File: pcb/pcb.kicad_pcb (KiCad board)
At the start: 2 copper layers, 48 x 60 mm, 47 parts, among them J1 USB_C_Receptacle_USB2.0_14P, J2 LCD, J4 LCD CTRL, J5 M SEN, J6 HC-05, J7 DEBUG, J9 USART3 TX, SW1 PWR SWITCH, U1 TLV62569DBV, U2 STM32F446RETx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

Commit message: finish revision 2
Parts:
- added FB1: FerriteBead, muRata BLM21PG121SN1D:BEADC2012X105N, F.Cu at (73.7, 88.9)
- added R10: 1, Resistor_SMD:R_0603_1608Metric_Pad0.98x0.95mm_HandSolder, F.Cu at (74.6, 85.9)
- D2: value SYS LED -> DEBUG LED
- J5: value M SEN -> MOISTURE
- J9: value USART3 TX -> DEBUG TX
- moved C12 1.48 mm to (77.8, 89.9)
- moved D3 1.48 mm to (79.8, 94.4)
- moved BT1 1.48 mm to (89.7, 91.0)
- moved C11 1.48 mm to (84.8, 89.7)
- moved R9 1.48 mm to (79.8, 92.6)
- moved U3 1.48 mm to (81.2, 89.7)
- moved R8 1.48 mm to (82.5, 93.4)
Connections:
- J1 pad A9: +Vext -> Net-(FB1-Pad1)
- J1 pad B9: +Vext -> Net-(FB1-Pad1)
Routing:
- net LCD D1: track 8.84 -> 19.1 mm, vias 1 -> 2
- net Net-(FB1-Pad1): track 0.00 -> 5.92 mm
- net +Vext: track 22.5 -> 16.6 mm
- net +Vbat: track 24.1 -> 19.4 mm
- net Net-(FB1-Pad2): track 0.00 -> 2.09 mm
- net +3.3V: track 94.9 -> 96.3 mm
- net GND: track 16.5 -> 16.7 mm, vias 46 -> 92
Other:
- board text added: "+3.3V"
- board text added: "+5V"
- board text added: "ADC2"
- board text added: "BLE"
- board text added: "CHARGE"
- board text added: "D0"
- board text added: "D1"
- board text added: "D2"
- board text added: "D3"
- board text added: "D4"
- board text added: "D5"
- board text added: "D6"
- board text added: "D7"
- board text added: "GND"
- board text added: "LCD"
- board text added: "LCD E"
- board text added: "LCD RS"
- board text added: "NRST"
- board text added: "POWER"
- board text added: "RX"
- board text added: "SWCLK"
- board text added: "SWDIO"
- board text added: "TX"
- board text added: "V0"
- board text added: "ed123213"

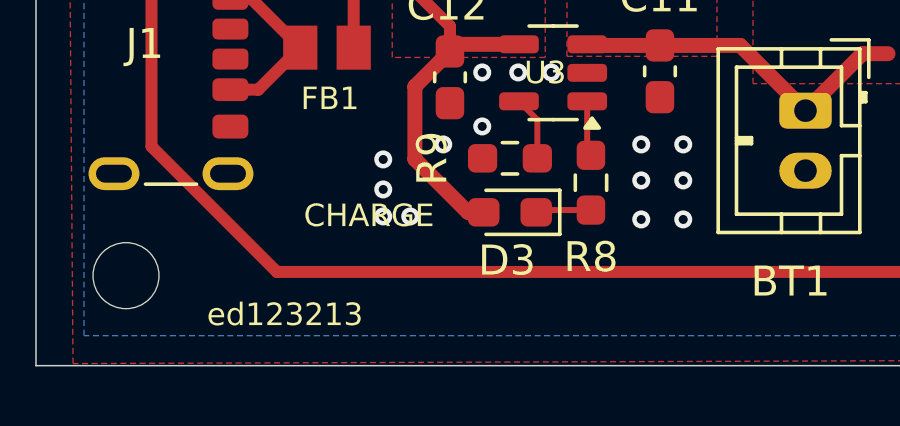
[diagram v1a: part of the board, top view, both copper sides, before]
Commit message: Add rev number to board
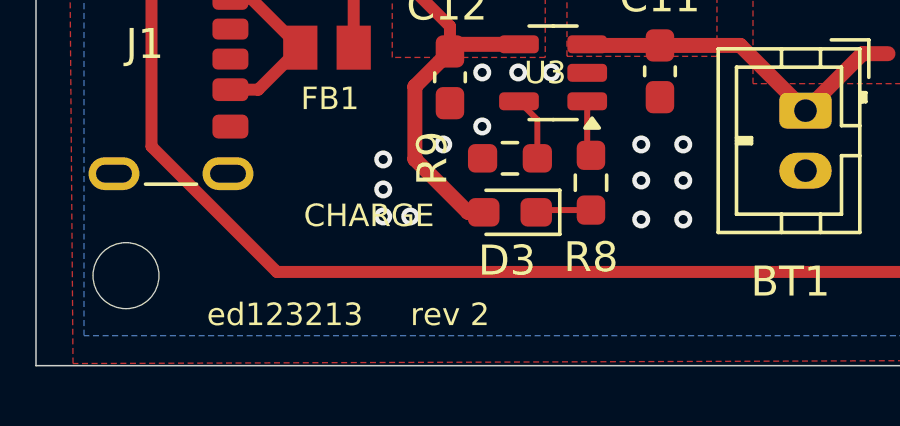
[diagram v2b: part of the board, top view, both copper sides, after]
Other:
- board text added: "rev 2"
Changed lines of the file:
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@@
+		)
+	)
+	(gr_text "rev 2"
+		(at 77.8 97.8 0)
+		(layer "F.SilkS")
+		(effects
+			(font
+				(size 0.75 0.75)
+				(thickness 0.09375)
+			)
 		)
 	)

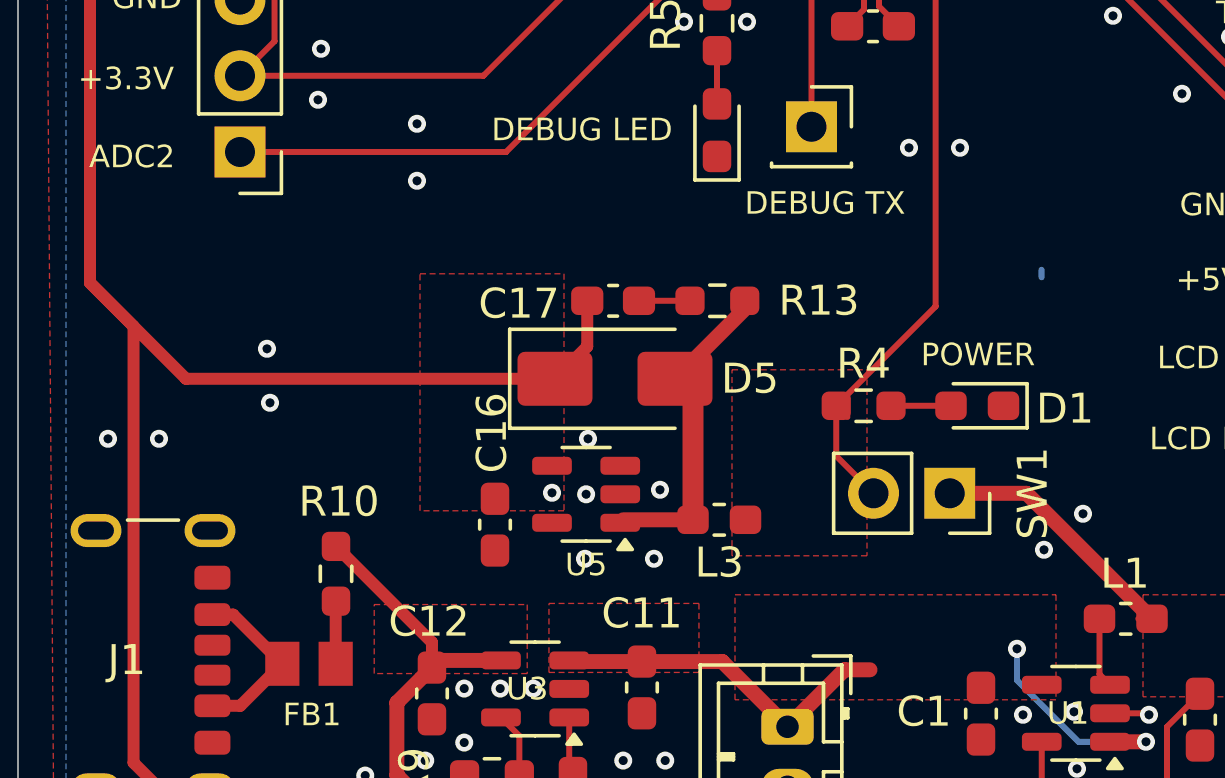
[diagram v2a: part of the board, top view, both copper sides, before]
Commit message: add power plane on boost converter input
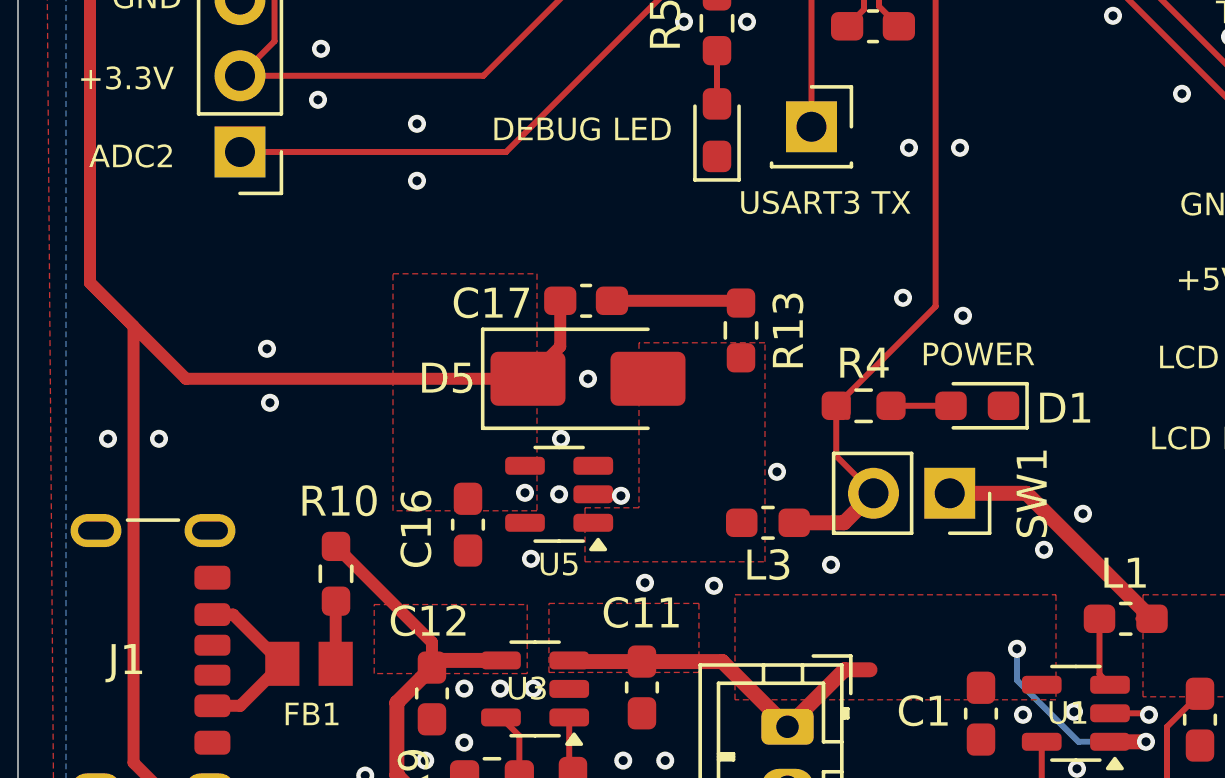
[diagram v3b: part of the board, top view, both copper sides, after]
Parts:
- J9: value DEBUG TX -> USART3 TX
- moved L3 1.63 mm to (89.0, 84.2)
- moved R13 1.26 mm to (88.1, 77.8), turned to 90 degrees
- moved C16 0.90 mm to (79.0, 84.3)
- moved C17 0.90 mm to (82.9, 76.8)
- moved D5 0.90 mm to (83.0, 79.4)
- moved U5 0.90 mm to (82.0, 83.2)
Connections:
- net SYS LED renamed DEBUG LED
- R1 pad 2: +3.3Vswin -> Net-(U1-FB)
- R2 pad 1: +3.3Vswin -> Net-(U1-FB)
- U1 pad 5: +3.3Vswin -> Net-(U1-FB)
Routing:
- net Net-(D5-A): track 11.3 -> 1.26 mm
- net +3.3Vswin: track 21.3 -> 17.5 mm
- net Net-(U1-FB): track 0.00 -> 3.79 mm
- net +3.3V: track 96.3 -> 99.3 mm
- net Net-(C17-Pad1): track 1.70 -> 4.33 mm
- net +5V: track 161.4 -> 160.5 mm
- net GND: track 16.7 -> 16.5 mm, vias 92 -> 98
- added copper zone on F.Cu, net Net-(D5-A)
- removed copper zone on F.Cu, net +3.3V

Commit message: mark pin 1 on stm32f4
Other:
- board text added: "1"
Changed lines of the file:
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@@
+		)
+	)
+	(gr_text "1"
+		(at 85 54.6 0)
+		(layer "F.SilkS")
+		(effects
+			(font
+				(size 0.7 0.7)
+				(thickness 0.15)
+			)
 		)
 	)

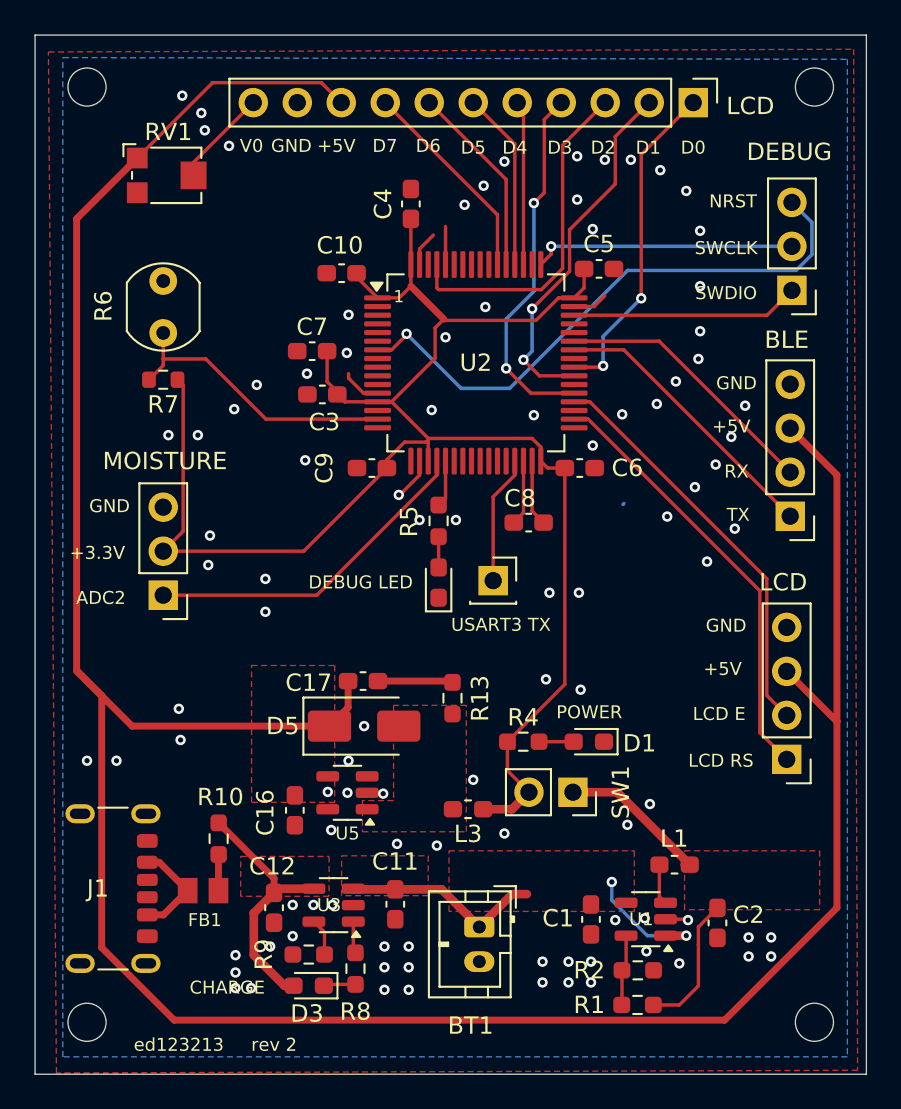
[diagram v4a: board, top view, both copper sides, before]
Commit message: Add battery sensor to pcb
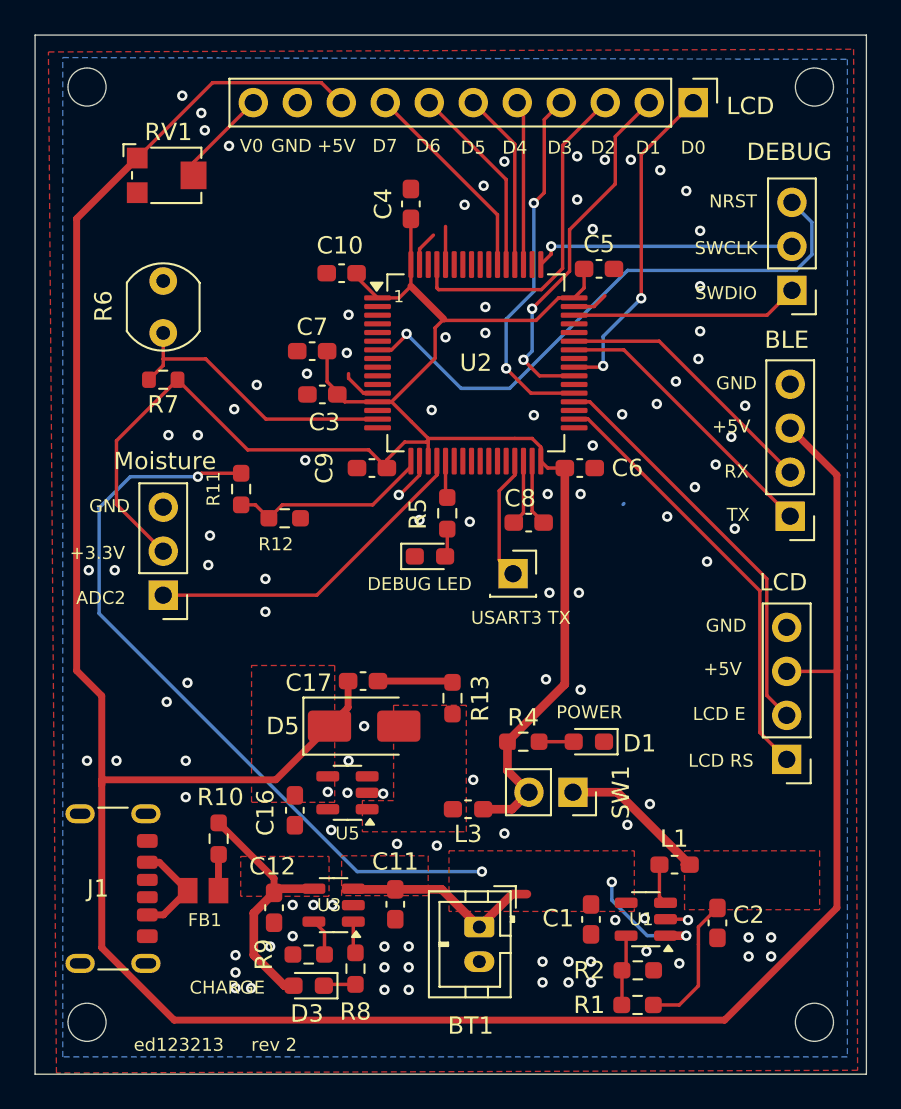
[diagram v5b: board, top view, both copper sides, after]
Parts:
- added R11: 100k, Resistor_SMD:R_0603_1608Metric_Pad0.98x0.95mm_HandSolder, F.Cu at (75.9, 65.7)
- added R12: 100k, Resistor_SMD:R_0603_1608Metric_Pad0.98x0.95mm_HandSolder, F.Cu at (78.4, 67.4)
- J5: value MOISTURE -> Moisture
- moved D2 1.59 mm to (86.8, 69.6), turned to 0 degrees
- moved J9 1.22 mm to (91.6, 70.6)
- moved R5 0.66 mm to (87.8, 67.1)
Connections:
- U2 pad 17: unconnected-(U2-PA3-Pad17) -> ADC3
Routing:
- net +Vbat: track 19.4 -> 62.8 mm, vias 2 -> 4
- net ADC3: track 0.00 -> 11.7 mm
- net +5V: track 160.5 -> 158.1 mm
- net +3.3V: track 99.3 -> 100.6 mm
- net DEBUG LED: track 2.70 -> 2.14 mm
- net GND: vias 98 -> 105

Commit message: Make power traces better on pcb
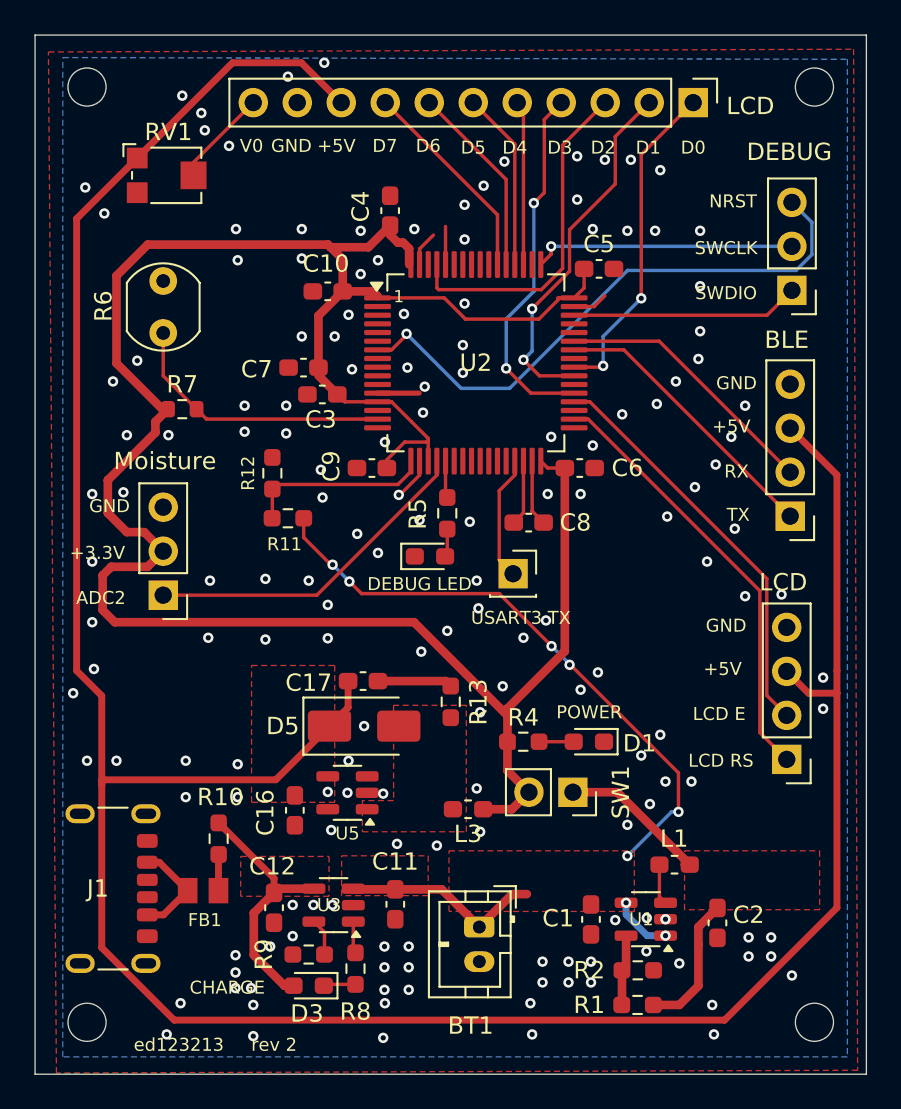
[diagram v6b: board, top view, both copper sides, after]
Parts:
- moved R11 3.18 mm to (78.6, 67.4), turned to 180 degrees
- moved R12 2.70 mm to (77.7, 64.8), turned to 90 degrees
- moved R7 2.02 mm to (72.5, 61.1), turned to 0 degrees
- moved C10 1.32 mm to (80.9, 54.3)
- moved C4 1.26 mm to (84.5, 49.6)
- moved C7 1.07 mm to (79.5, 58.7)
- moved R13 0.23 mm to (88.0, 78.0)
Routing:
- net +3.3V: track 100.6 -> 137.1 mm
- net +Vbat: track 62.8 -> 50.1 mm, vias 4 -> 8
- net +5V: track 158.1 -> 159.5 mm
- net GND: track 16.5 -> 15.2 mm, vias 105 -> 163
- net ADC1: track 16.9 -> 15.9 mm
- net ADC3: track 11.7 -> 10.7 mm

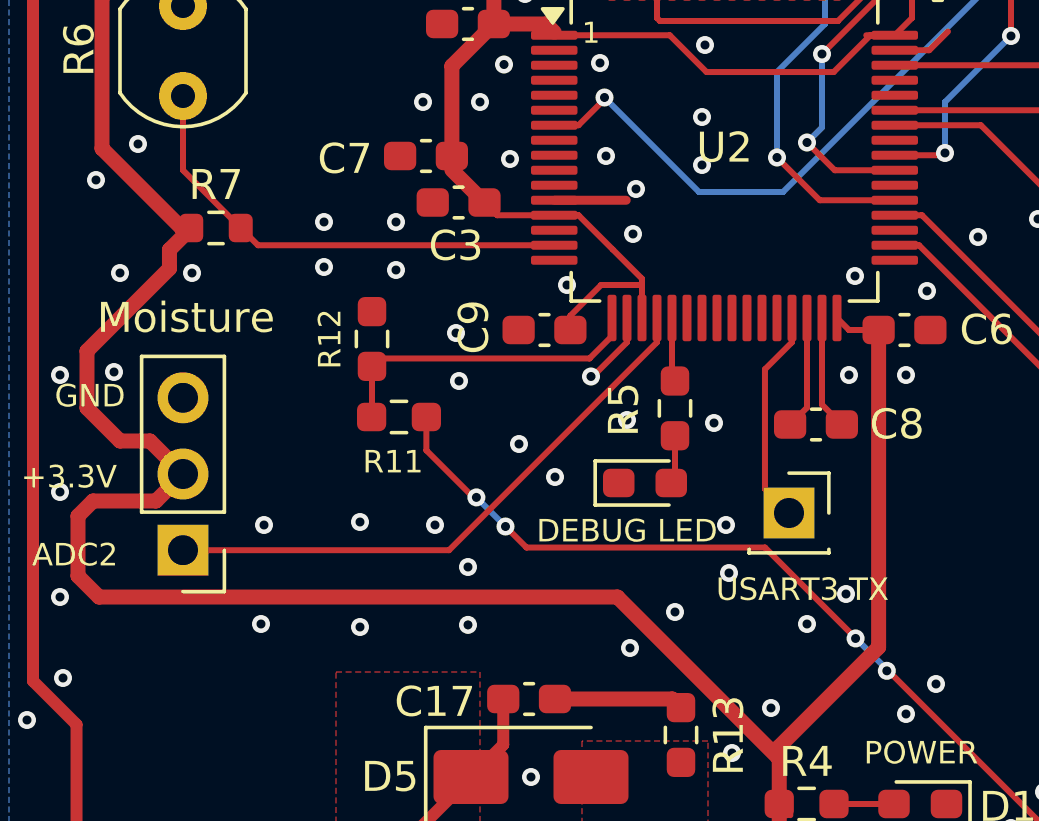
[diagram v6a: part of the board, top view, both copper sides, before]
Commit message: Add pcb export to makefile
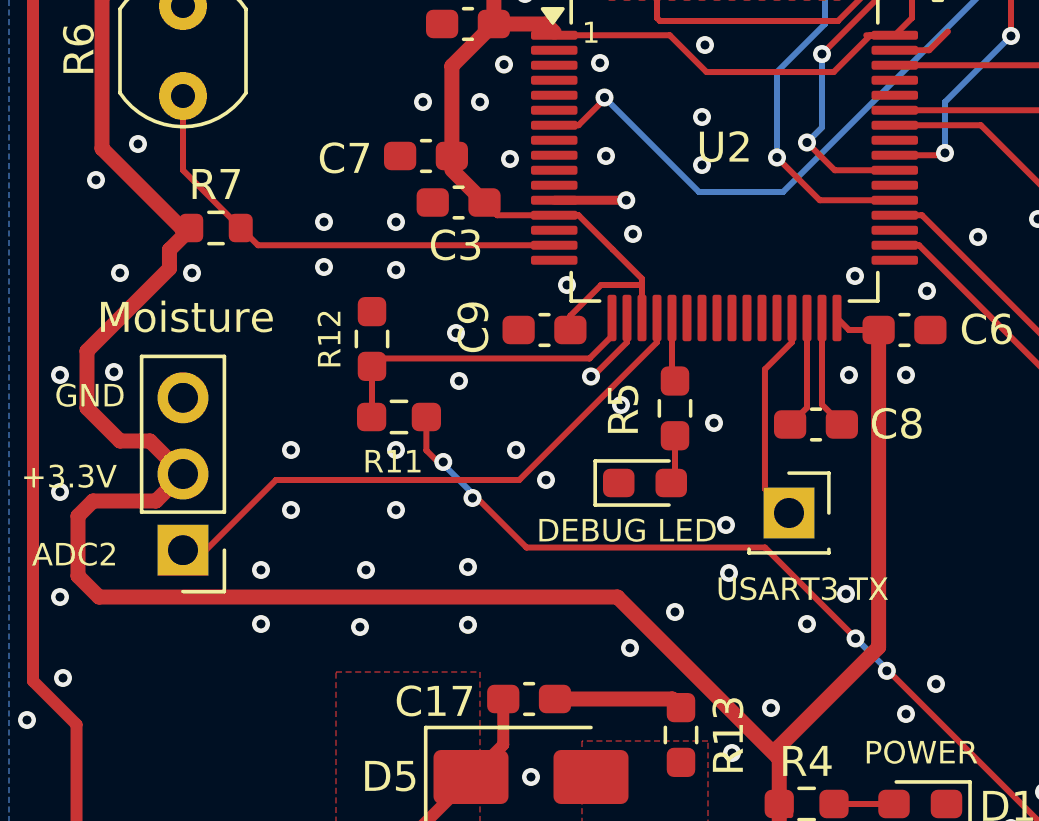
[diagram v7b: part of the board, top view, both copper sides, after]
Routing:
- net GND: vias 163 -> 166
